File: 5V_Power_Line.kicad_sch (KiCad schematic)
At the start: 26 parts, among them Q5 CSD18543Q3A, Q6 CSD18543Q3A, U7 LM25145RGYR

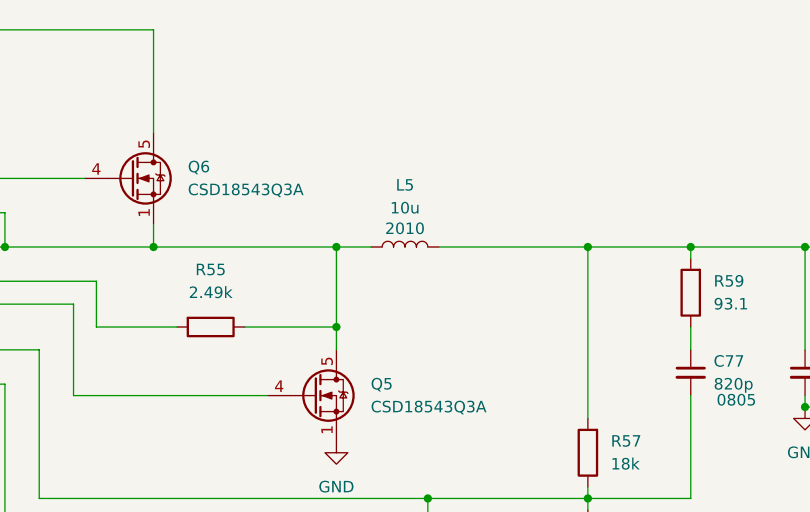
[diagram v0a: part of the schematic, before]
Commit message: 20V line PCB v1
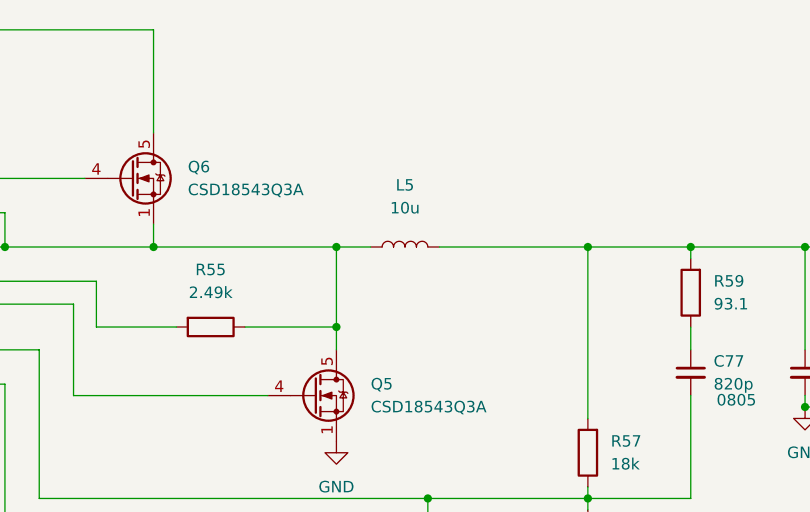
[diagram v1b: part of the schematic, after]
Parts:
- L5: footprint Inductor_SMD_Wurth:L_Wurth_WE-LQSH-2010 -> Inductor_THT:L_Radial_D10.0mm_P5.00mm_Fastron_07M
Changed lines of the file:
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@@
 			)
 		)
-		(property "Footprint" "Inductor_SMD_Wurth:L_Wurth_WE-LQSH-2010"
+		(property "Footprint" "Inductor_THT:L_Radial_D10.0mm_P5.00mm_Fastron_07M"
 			(at 215.9 87.63 0)
 			(effects
@@
 			)
 		)
-		(property "Description" "2010"
+		(property "Description" "6mm x 6mm"
 			(at 215.9 85.598 90)
 			(effects
@@
 					(size 1.27 1.27)
 				)
+				(hide yes)
 			)
 		)
